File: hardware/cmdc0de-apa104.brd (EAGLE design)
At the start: 101.6 x 74.6 mm, 128 parts, among them IC1 ATTINY13A-SSU

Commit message: no errors board is complete?
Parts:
- removed J2: (no value), name-in-lights:1X02
- added POWER-IN: 5V, name-in-lights:1X02
- APA104-1, APA104-10, APA104-11, APA104-12, APA104-13, APA104-14, APA104-15, APA104-16, APA104-17, APA104-18, APA104-19, APA104-2, APA104-20, APA104-21, APA104-22, APA104-23, APA104-24, APA104-25, APA104-26, APA104-27, APA104-28, APA104-29, APA104-3, APA104-30, APA104-31, APA104-32, APA104-33, APA104-34, APA104-35, APA104-36, APA104-37, APA104-38, APA104-39, APA104-4, APA104-40, APA104-41, APA104-42, APA104-43, APA104-44, APA104-45, APA104-46, APA104-47, APA104-48, APA104-49, APA104-5, APA104-50, APA104-51, APA104-52, APA104-53, APA104-54, APA104-55, APA104-56, APA104-57, APA104-58, APA104-59, APA104-6, APA104-60, APA104-7, APA104-8, APA104-9: device dc-26:APA104 -> name-in-lights:APA104
- C-L-10, C-L-11, C-L-12, C-L-13, C-L-14, C-L-15, C-L-16, C-L-17, C-L-18, C-L-19, C-L-2, C-L-20, C-L-21, C-L-22, C-L-23, C-L-24, C-L-25, C-L-26, C-L-27, C-L-28, C-L-29, C-L-3, C-L-30, C-L-31, C-L-32, C-L-33, C-L-34, C-L-35, C-L-36, C-L-37, C-L-38, C-L-39, C-L-4, C-L-40, C-L-41, C-L-42, C-L-43, C-L-44, C-L-45, C-L-46, C-L-47, C-L-48, C-L-49, C-L-5, C-L-50, C-L-51, C-L-52, C-L-53, C-L-54, C-L-55, C-L-56, C-L-57, C-L-58, C-L-59, C-L-6, C-L-60, C-L-7, C-L-8, C-L9: value (none) -> 15pf
- C81, C82, C83: device NameInLights:C0805 -> name-in-lights:C0805-VOLTA
- J1: value (none) -> 1x8 header
- moved C-L-58 136.3 mm to (96.0, 58.5)
- moved C-L-59 134.4 mm to (94.0, 55.0)
- moved C-L-60 130.1 mm to (95.0, 43.0)
- moved C-L-57 128.4 mm to (88.0, 59.0), turned to 180 degrees
- moved C-L-56 122.5 mm to (88.5, 51.0), turned to 180 degrees
- moved C-L-55 120.7 mm to (91.2, 46.0), turned to 90 degrees
- moved C-L-54 114.2 mm to (91.0, 35.0)
- moved C-L-27 110.4 mm to (94.8, 89.8)
- moved C-L-26 106.8 mm to (91.2, 92.2), turned to 90 degrees
- moved C-L-50 106.6 mm to (74.8, 61.0), turned to 90 degrees
- moved C-L-28 103.4 mm to (88.5, 81.8), turned to 90 degrees
- moved C-L-51 103.3 mm to (72.5, 55.5), turned to 270 degrees
- moved C-L-29 101.7 mm to (87.0, 77.2)
- moved C-L-52 101.2 mm to (72.5, 48.5), turned to 270 degrees
- moved C-L-25 100.2 mm to (85.8, 86.0), turned to 270 degrees
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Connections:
- removed net GPIO_APA106_DATA: J1.7
- removed net N$69: APA104-60.2
- removed net VCC: C81.2, C82.2, IC1.8, J1.1, J2.1, R1.1
- removed net VCC5V: APA104-1.1, APA104-10.1, APA104-11.1, APA104-12.1, APA104-13.1, APA104-14.1, APA104-15.1, APA104-16.1, APA104-17.1, APA104-18.1, APA104-19.1, APA104-2.1, APA104-20.1, APA104-21.1, APA104-22.1, APA104-23.1, APA104-24.1, APA104-25.1, APA104-26.1, APA104-27.1, APA104-28.1, APA104-29.1, APA104-3.1, APA104-30.1, APA104-31.1, APA104-32.1, APA104-33.1, APA104-34.1, APA104-35.1, APA104-36.1, APA104-37.1, APA104-38.1, APA104-39.1, APA104-4.1, APA104-40.1, APA104-41.1, APA104-42.1, APA104-43.1, APA104-44.1, APA104-45.1, APA104-46.1, APA104-47.1, APA104-48.1, APA104-49.1, APA104-5.1, APA104-50.1, APA104-51.1, APA104-52.1, APA104-53.1, APA104-54.1, APA104-55.1, APA104-56.1, APA104-57.1, APA104-58.1, APA104-59.1, APA104-6.1, APA104-60.1, APA104-7.1, APA104-8.1, APA104-9.1, C-L-1.2, C-L-10.1, C-L-11.1, C-L-12.1, C-L-13.1, C-L-14.1, C-L-15.1, C-L-16.1, C-L-17.1, C-L-18.1, C-L-19.1, C-L-2.1, C-L-20.1, C-L-21.1, C-L-22.1, C-L-23.1, C-L-24.1, C-L-25.1, C-L-26.1, C-L-27.1, C-L-28.1, C-L-29.1, C-L-3.1, C-L-30.1, C-L-31.1, C-L-32.1, C-L-33.1, C-L-34.1, C-L-35.1, C-L-36.1, C-L-37.1, C-L-38.1, C-L-39.1, C-L-4.1, C-L-40.1, C-L-41.1, C-L-42.1, C-L-43.1, C-L-44.1, C-L-45.1, C-L-46.1, C-L-47.1, C-L-48.1, C-L-49.1, C-L-5.1, C-L-50.1, C-L-51.1, C-L-52.1, C-L-53.1, C-L-54.1, C-L-55.1, C-L-56.1, C-L-57.1, C-L-58.1, C-L-59.1, C-L-6.1, C-L-60.1, C-L-7.1, C-L-8.1, C-L9.1
- new net VDD: APA104-1.1, APA104-10.1, APA104-11.1, APA104-12.1, APA104-13.1, APA104-14.1, APA104-15.1, APA104-16.1, APA104-17.1, APA104-18.1, APA104-19.1, APA104-2.1, APA104-20.1, APA104-21.1, APA104-22.1, APA104-23.1, APA104-24.1, APA104-25.1, APA104-26.1, APA104-27.1, APA104-28.1, APA104-29.1, APA104-3.1, APA104-30.1, APA104-31.1, APA104-32.1, APA104-33.1, APA104-34.1, APA104-35.1, APA104-36.1, APA104-37.1, APA104-38.1, APA104-39.1, APA104-4.1, APA104-40.1, APA104-41.1, APA104-42.1, APA104-43.1, APA104-44.1, APA104-45.1, APA104-46.1, APA104-47.1, APA104-48.1, APA104-49.1, APA104-5.1, APA104-50.1, APA104-51.1, APA104-52.1, APA104-53.1, APA104-54.1, APA104-55.1, APA104-56.1, APA104-57.1, APA104-58.1, APA104-59.1, APA104-6.1, APA104-60.1, APA104-7.1, APA104-8.1, APA104-9.1, C-L-1.2, C-L-10.1, C-L-11.1, C-L-12.1, C-L-13.1, C-L-14.1, C-L-15.1, C-L-16.1, C-L-17.1, C-L-18.1, C-L-19.1, C-L-2.1, C-L-20.1, C-L-21.1, C-L-22.1, C-L-23.1, C-L-24.1, C-L-25.1, C-L-26.1, C-L-27.1, C-L-28.1, C-L-29.1, C-L-3.1, C-L-30.1, C-L-31.1, C-L-32.1, C-L-33.1, C-L-34.1, C-L-35.1, C-L-36.1, C-L-37.1, C-L-38.1, C-L-39.1, C-L-4.1, C-L-40.1, C-L-41.1, C-L-42.1, C-L-43.1, C-L-44.1, C-L-45.1, C-L-46.1, C-L-47.1, C-L-48.1, C-L-49.1, C-L-5.1, C-L-50.1, C-L-51.1, C-L-52.1, C-L-53.1, C-L-54.1, C-L-55.1, C-L-56.1, C-L-57.1, C-L-58.1, C-L-59.1, C-L-6.1, C-L-60.1, C-L-7.1, C-L-8.1, C-L9.1, C81.2, C82.2, IC1.8, J1.1, POWER-IN.1, R1.1
- net GND: now also POWER-IN.2; no longer J2.2
- net GPIO_APA104_DATA: now also J1.5
- net PB0-MOSI: now also J1.4; no longer J1.6
- net PB1-MISO: now also J1.3; no longer J1.5
- net PB2-SCK: now also J1.2; no longer J1.4
- net PB3: now also J1.6; no longer J1.3
- net RESET: now also J1.7; no longer J1.2
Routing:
- net VDD: track 0.00 -> 1082.9 mm, vias 0 -> 3
- net GPIO_APA104_DATA: track 0.00 -> 150.1 mm
- net N$27: track 0.00 -> 65.4 mm
- net RESET: track 0.00 -> 31.0 mm
- net PB2-SCK: track 0.00 -> 23.0 mm
- net PB1-MISO: track 0.00 -> 20.0 mm
- net PB3: track 0.00 -> 19.7 mm
- net N$45: track 0.00 -> 18.7 mm
- net PB0-MOSI: track 0.00 -> 17.5 mm
- net N$53: track 0.00 -> 17.3 mm
- net N$19: track 0.00 -> 14.8 mm
- net N$24: track 0.00 -> 13.8 mm
- net N$58: track 0.00 -> 12.7 mm
- net N$7: track 0.00 -> 12.4 mm
- net N$30: track 0.00 -> 12.2 mm
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- added copper zone on layer 1, net GND
- added copper zone on layer 16, net GND

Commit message: fixed wire pieces
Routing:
- net VDD: track 1082.9 -> 1079.3 mm
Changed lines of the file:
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@@
 <contactref element="C-L-59" pad="1"/>
 <contactref element="C-L-60" pad="1"/>
-<wire x1="16.8" y1="96.6" x2="14" y2="96.6" width="0.254" layer="1"/>
-<wire x1="14" y1="96.6" x2="13.6" y2="96.6" width="0.254" layer="1"/>
-<wire x1="9.1" y1="94.1" x2="9" y2="94" width="0.254" layer="1"/>
+<wire x1="16.8" y1="96.6" x2="13.3613125" y2="96.6" width="0.254" layer="1"/>
 <wire x1="6.8636" y1="87.7564" x2="7.02" y2="87.6" width="0.254" layer="1"/>
-<wire x1="10.7836" y1="73.8636" x2="11.02" y2="74.1" width="0.254" layer="1"/>
-<wire x1="24.7436" y1="70.6364" x2="24.69" y2="70.69" width="0.254" layer="1"/>
-<wire x1="24.69" y1="70.69" x2="24.48" y2="70.9" width="0.254" layer="1"/>
-<wire x1="24.7436" y1="70.6364" x2="24.69" y2="70.69" width="0.254" layer="1"/>
-<wire x1="24.69" y1="70.69" x2="24.48" y2="70.9" width="0.254" layer="1"/>
+<wire x1="24.769" y1="70.611" x2="24.48" y2="70.9" width="0.254" layer="1"/>
 <contactref element="IC1" pad="8"/>
 <contactref element="C81" pad="2"/>
@@
 <wire x1="12.6310125" y1="95.8697" x2="11.1469875" y2="95.8697" width="0.254" layer="1"/>
 <wire x1="11.1469875" y1="95.8697" x2="10.9238" y2="96.0928875" width="0.254" layer="1"/>
-<wire x1="14" y1="96.6" x2="13.3613125" y2="96.6" width="0.254" layer="1"/>
 <wire x1="10.9238" y1="96.0928875" x2="10.9238" y2="96.1872" width="0.254" layer="1"/>
 <wire x1="13.3613125" y1="96.6" x2="12.6310125" y2="95.8697" width="0.254" layer="1"/>
 <wire x1="10.9238" y1="96.1872" x2="10.111" y2="97" width="0.254" layer="1"/>
 <wire x1="10.111" y1="97" x2="10.111" y2="95.111" width="0.254" layer="1"/>
-<wire x1="10.111" y1="95.111" x2="9" y2="94" width="0.254" layer="1"/>
+<wire x1="10.111" y1="95.111" x2="9.1" y2="94.1" width="0.254" layer="1"/>
 <wire x1="27" y1="70.611" x2="31.800875" y2="70.611" width="0.254" layer="1"/>
 <wire x1="37.066" y1="69.934" x2="38" y2="69" width="0.254" layer="1"/>
@@
 <wire x1="32.477875" y1="69.934" x2="37.066" y2="69.934" width="0.254" layer="1"/>
 <wire x1="38" y1="69" x2="40.889" y2="69" width="0.254" layer="1"/>
-<wire x1="41.301" y1="71.111" x2="41.095" y2="70.905" width="0.254" layer="1"/>
 <wire x1="41.095" y1="70.905" x2="40.98" y2="70.79" width="0.254" layer="1"/>
 <wire x1="43.5" y1="77.611" x2="43.469" y2="77.58" width="0.254" layer="1"/>
@@
 <wire x1="46" y1="89" x2="47.639440625" y2="89" width="0.254" layer="1"/>
 <wire x1="47.639440625" y1="89" x2="48.804053125" y2="90.1646125" width="0.254" layer="1"/>
-<wire x1="48.804053125" y1="90.1646125" x2="49" y2="89.968665625" width="0.254" layer="1"/>
 <wire x1="44.617503125" y1="84.617503125" x2="44.4273375" y2="84.617503125" width="0.254" layer="1"/>
-<wire x1="46.5" y1="68.889" x2="46.6945" y2="68.6945" width="0.254" layer="1"/>
-<wire x1="46.6945" y1="68.6945" x2="46.889" y2="68.5" width="0.254" layer="1"/>
+<wire x1="46.5" y1="68.889" x2="46.889" y2="68.5" width="0.254" layer="1"/>
 <wire x1="48.804053125" y1="90.1646125" x2="44.4273375" y2="85.787896875" width="0.254" layer="1"/>
 <wire x1="44.4273375" y1="85.787896875" x2="44.4273375" y2="84.617503125" width="0.254" layer="1"/>
@@
 <wire x1="42.1197" y1="73.6310125" x2="43" y2="74.5113125" width="0.254" layer="1"/>
 <wire x1="43.25" y1="71.111" x2="42.4372" y2="71.9238" width="0.254" layer="1"/>
-<wire x1="58.216003125" y1="77.997334375" x2="58.554053125" y2="78.335384375" width="0.254" layer="1"/>
 <wire x1="58.554053125" y1="78.335384375" x2="58.554053125" y2="78.445946875" width="0.254" layer="1"/>
 <wire x1="58.554053125" y1="78.445946875" x2="57" y2="80" width="0.254" layer="1"/>
@@
 <wire x1="6.889" y1="87.7818" x2="6.8636" y2="87.7564" width="0.254" layer="1"/>
 <wire x1="6.889" y1="90" x2="6.889" y2="91.889" width="0.254" layer="1"/>
-<wire x1="6.889" y1="91.889" x2="9" y2="94" width="0.254" layer="1"/>
+<wire x1="6.889" y1="91.889" x2="9.1" y2="94.1" width="0.254" layer="1"/>
 <wire x1="8.5" y1="74.7311875" x2="8.5" y2="73.889" width="0.254" layer="1"/>
 <wire x1="6.464" y1="76.7671875" x2="8.5" y2="74.7311875" width="0.254" layer="1"/>
 <wire x1="6.464" y1="76.7671875" x2="6.464" y2="79.5193125" width="0.254" layer="1"/>
 <wire x1="8.5" y1="73.889" x2="9" y2="73.889" width="0.254" layer="1"/>
-<wire x1="9" y1="73.889" x2="10.809" y2="73.889" width="0.254" layer="1"/>
-<wire x1="10.809" y1="73.889" x2="11.02" y2="74.1" width="0.254" layer="1"/>
 <wire x1="11.11559375" y1="69.11559375" x2="9.6303" y2="70.6008875" width="0.254" layer="1"/>
 <wire x1="9" y1="73.4833125" x2="9" y2="73.889" width="0.254" layer="1"/>
@@
 <wire x1="9.6303" y1="72.8530125" x2="9" y2="73.4833125" width="0.254" layer="1"/>
 <wire x1="27" y1="70.611" x2="24.769" y2="70.611" width="0.254" layer="1"/>
-<wire x1="24.769" y1="70.611" x2="24.69" y2="70.69" width="0.254" layer="1"/>
 <wire x1="27" y1="70.611" x2="27.8128" y2="71.4238" width="0.254" layer="1"/>
 <wire x1="27.8128" y1="71.4238" x2="27.9071125" y2="71.4238" width="0.254" layer="1"/>
-<wire x1="28.8697" y1="73.3530125" x2="29.0928875" y2="73.5762" width="0.254" layer="1"/>
 <wire x1="27.9071125" y1="71.4238" x2="28.8697" y2="72.3863875" width="0.254" layer="1"/>
-<wire x1="28.8697" y1="72.3863875" x2="28.8697" y2="73" width="0.254" layer="1"/>
-<wire x1="28.8697" y1="73" x2="28.8697" y2="73.3530125" width="0.254" layer="1"/>
+<wire x1="28.8697" y1="72.3863875" x2="28.8697" y2="73.3530125" width="0.254" layer="1"/>
 <wire x1="46.889" y1="68.5" x2="48.903" y2="70.514" width="0.254" layer="1"/>
 <wire x1="48.903" y1="70.514" x2="49.5128125" y2="70.514" width="0.254" layer="1"/>
@@
 <wire x1="12.389" y1="65" x2="14.5" y2="65" width="0.254" layer="1"/>
 <wire x1="14.5" y1="65" x2="14.9" y2="64.6" width="0.254" layer="1"/>
-<wire x1="4.25" y1="62.25" x2="4.25" y2="62.139" width="0.254" layer="1"/>
-<wire x1="4.25" y1="62.139" x2="4.461" y2="62.35" width="0.254" layer="1"/>
 <wire x1="3" y1="47.639" x2="5.141" y2="47.639" width="0.254" layer="1"/>
 <wire x1="5.141" y1="47.639" x2="5.18" y2="47.6" width="0.254" layer="1"/>
@@
 <wire x1="94.111" y1="43" x2="92.5" y2="41.389" width="0.254" layer="1"/>
 <wire x1="92.5" y1="41.389" x2="92.5" y2="40.6" width="0.254" layer="1"/>
-<wire x1="37.009" y1="38.241" x2="37" y2="38.241" width="0.254" layer="1"/>
 <wire x1="37" y1="38.241" x2="36.49" y2="38.241" width="0.254" layer="1"/>
-<wire x1="33.91" y1="37.991" x2="33.74" y2="38.161" width="0.254" layer="1"/>
-<wire x1="33.74" y1="38.161" x2="33.9505" y2="37.9505" width="0.254" layer="1"/>
 <contactref element="J1" pad="1"/>
-<wire x1="33.9505" y1="37.9505" x2="34.022" y2="37.879" width="0.254" layer="1"/>
 <contactref element="R1" pad="1"/>
 <via x="27" y="36" extent="1-16" drill="0.4"/>
-<wire x1="36.49" y1="38.241" x2="34.241" y2="38.241" width="0.254" layer="1"/>
-<wire x1="34.241" y1="38.241" x2="33.9505" y2="37.9505" width="0.254" layer="1"/>
-<wire x1="33.74" y1="38.161" x2="35.772" y2="36.129" width="0.254" layer="1"/>
-<wire x1="35.772" y1="36.129" x2="35.772" y2="35.215" width="0.254" layer="1"/>
 <via x="38" y="37" extent="1-16" drill="0.4"/>
 <via x="60" y="35" extent="1-16" drill="0.4"/>
@@
 <wire x1="49.559" y1="52.389" x2="49.84" y2="52.67" width="0.254" layer="1"/>
 <wire x1="7.52" y1="80.6" x2="7.6" y2="80.6" width="0.254" layer="1"/>
-<wire x1="7.6" y1="80.6" x2="8" y2="81" width="0.254" layer="1"/>
+<wire x1="7.6" y1="80.6" x2="7.889" y2="80.889" width="0.254" layer="1"/>
 <wire x1="8" y1="81" x2="7.889" y2="80.889" width="0.254" layer="1"/>
 <wire x1="7.889" y1="80.889" x2="5" y2="80.889" width="0.254" layer="1"/>
 <wire x1="30" y1="74.1303" x2="30" y2="74.389" width="0.254" layer="1"/>
-<wire x1="28.8697" y1="73" x2="28.8697" y2="73.3530125" width="0.254" layer="1"/>
 <wire x1="28.8697" y1="73.3530125" x2="29.0928875" y2="73.5762" width="0.254" layer="1"/>
 <wire x1="29.0928875" y1="73.5762" x2="29.4459" y2="73.5762" width="0.254" layer="1"/>
@@
 <wire x1="40" y1="34.453" x2="38" y2="36.453" width="0.254" layer="1"/>
 <wire x1="38" y1="36.453" x2="38" y2="37" width="0.254" layer="1"/>
+<wire x1="8.5" y1="73.889" x2="10.809" y2="73.889" width="0.254" layer="1"/>
+<wire x1="10.809" y1="73.889" x2="11.02" y2="74.1" width="0.254" layer="1"/>
+<wire x1="36.49" y1="38.241" x2="36.41" y2="38.161" width="0.254" layer="1"/>
+<wire x1="36.41" y1="38.161" x2="33.74" y2="38.161" width="0.254" layer="1"/>
+<wire x1="33.74" y1="38.161" x2="35.772" y2="36.129" width="0.254" layer="1"/>
+<wire x1="35.772" y1="36.129" x2="35.772" y2="35.215" width="0.254" layer="1"/>
 </signal>
 <signal name="GPIO_APA104_DATA1">

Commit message: board and gerbers
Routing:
- net VDD: track 1079.3 -> 1078.4 mm
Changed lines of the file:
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@@
 <wire x1="46" y1="89" x2="47.639440625" y2="89" width="0.254" layer="1"/>
 <wire x1="47.639440625" y1="89" x2="48.804053125" y2="90.1646125" width="0.254" layer="1"/>
-<wire x1="44.617503125" y1="84.617503125" x2="44.4273375" y2="84.617503125" width="0.254" layer="1"/>
-<wire x1="46.5" y1="68.889" x2="46.889" y2="68.5" width="0.254" layer="1"/>
 <wire x1="48.804053125" y1="90.1646125" x2="44.4273375" y2="85.787896875" width="0.254" layer="1"/>
 <wire x1="44.4273375" y1="85.787896875" x2="44.4273375" y2="84.617503125" width="0.254" layer="1"/>
@@
 <wire x1="7.52" y1="80.6" x2="7.6" y2="80.6" width="0.254" layer="1"/>
 <wire x1="7.6" y1="80.6" x2="7.889" y2="80.889" width="0.254" layer="1"/>
-<wire x1="8" y1="81" x2="7.889" y2="80.889" width="0.254" layer="1"/>
 <wire x1="7.889" y1="80.889" x2="5" y2="80.889" width="0.254" layer="1"/>
 <wire x1="30" y1="74.1303" x2="30" y2="74.389" width="0.254" layer="1"/>

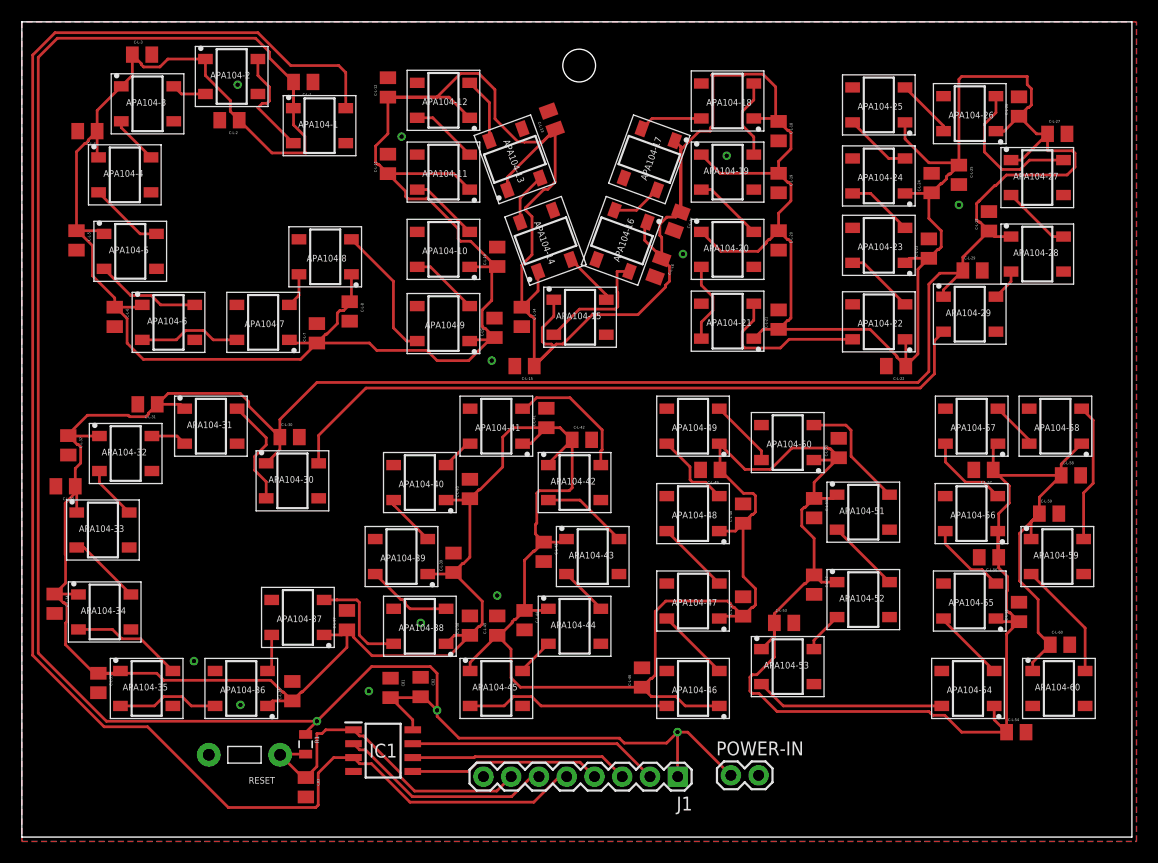
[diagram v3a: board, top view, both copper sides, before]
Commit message: added .7 mm as min diameter, removed gnd plane and traced them instead due to how voltera works
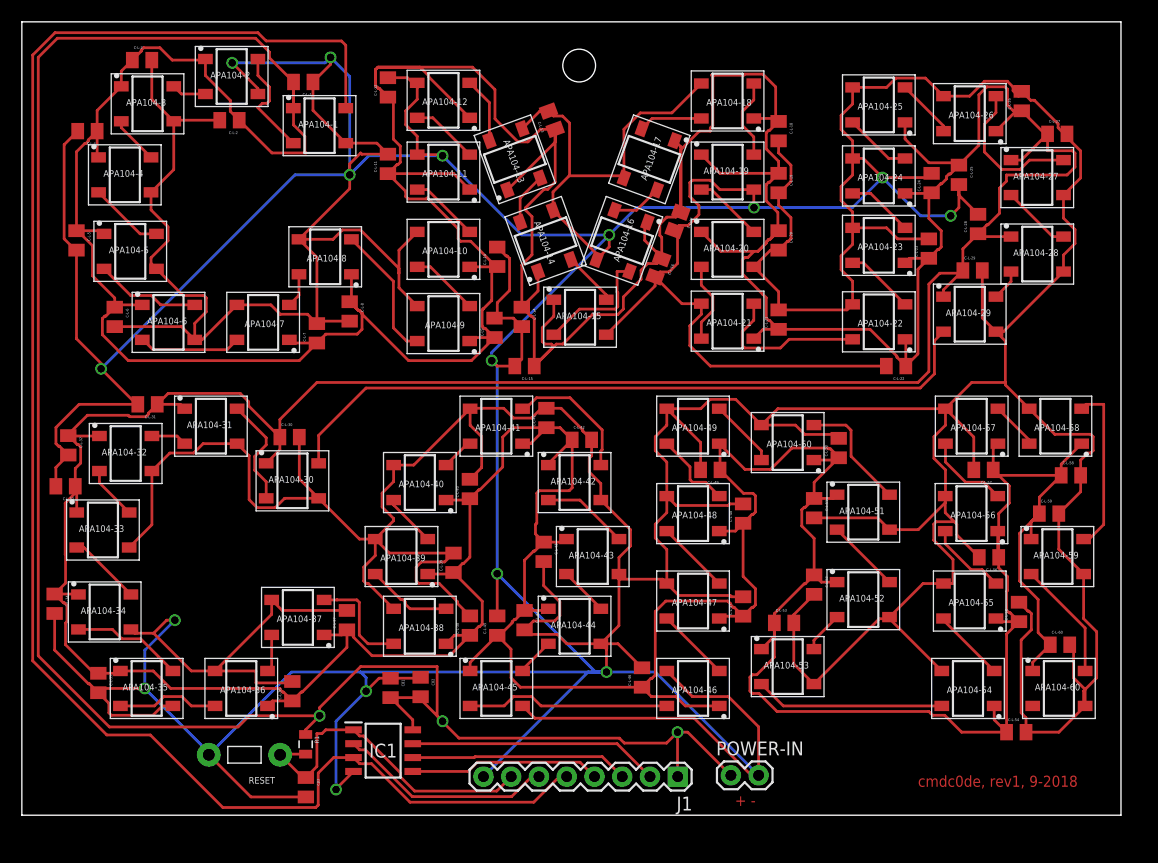
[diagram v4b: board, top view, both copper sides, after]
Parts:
- moved C-L-28 1.03 mm to (87.5, 81.5)
- moved C-L-26 0.56 mm to (91.5, 92.8)
- moved C-L-3 0.50 mm to (11.0, 96.5)
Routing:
- net GND: track 0.00 -> 1181.6 mm, vias 11 -> 16
- net VDD: track 1078.4 -> 1088.0 mm
- net N$58: track 12.7 -> 15.6 mm
- net GPIO_APA104_DATA: track 150.1 -> 151.9 mm
- removed copper zone on layer 1, net GND
- removed copper zone on layer 16, net GND
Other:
- board size 101.6 x 74.6 mm -> 100.6 x 72.6 mm
- board text added: "+ -"
- board text added: "cmdc0de, rev1, 9-2018"

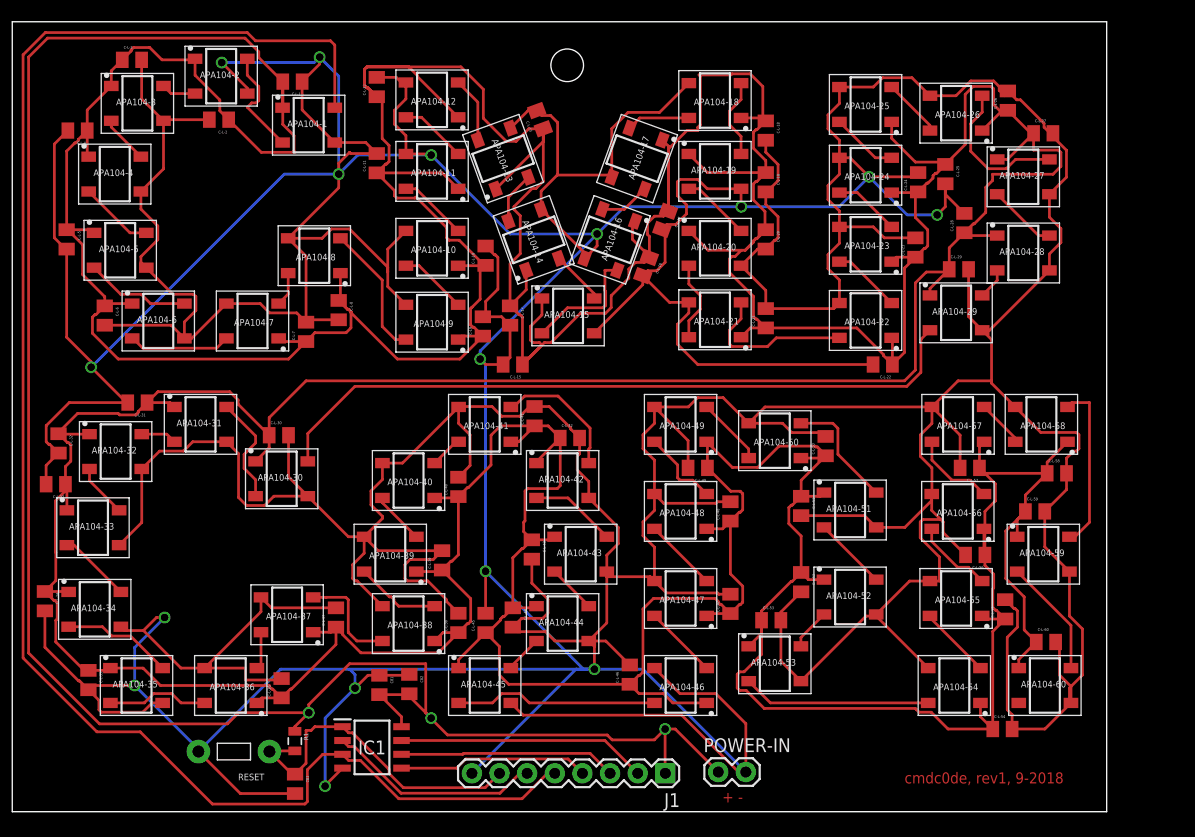
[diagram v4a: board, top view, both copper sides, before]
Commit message: spaced a few traces farther apart and got the rev as a larger font
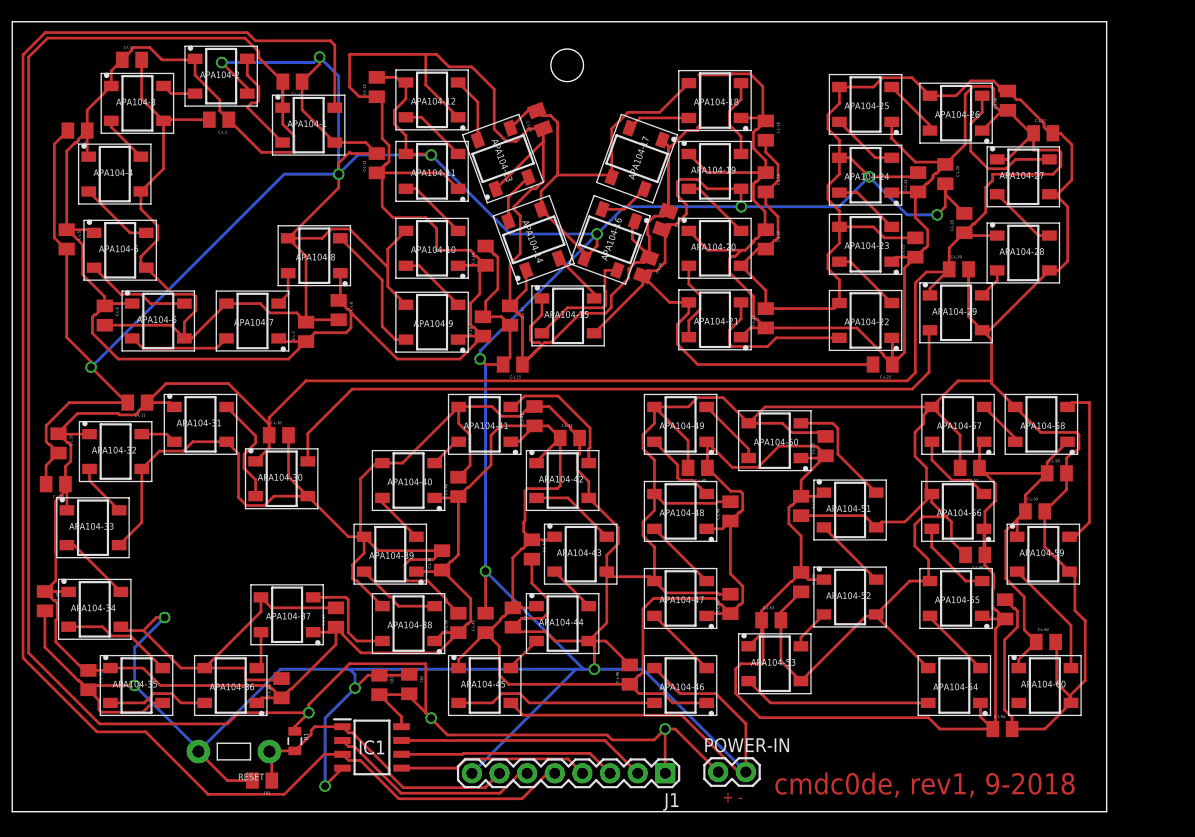
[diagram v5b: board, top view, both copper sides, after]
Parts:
- moved C83 3.04 mm to (23.0, 30.3), turned to 180 degrees
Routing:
- net GND: track 1181.6 -> 1176.5 mm
- net VDD: track 1088.0 -> 1084.5 mm
- net RESET: track 31.0 -> 28.2 mm
- net GPIO_APA104_DATA: track 151.9 -> 149.4 mm
